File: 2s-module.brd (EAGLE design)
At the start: 100 x 80 mm, 3 parts, among them J1 CQ-USB-C16PSMT01

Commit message: build balancer prototype
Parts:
- added C1: 1nF, Capacitor:CAPC1608X85
- added C2: 22uF, Capacitor:CAPC3216X135
- added C3, C4, C5: 10nF, Capacitor:CAPC1608X85
- added JP1: PINHD-1X3, Connector:1X03
- added L1: 0630CDMCCDS-4R7MC, 0630CDMCCDS-4R7MC:0630CDMCCDS-4R7MC
- added LED1: red, adafruit:CHIPLED_0603
- added R3: 1k, resistor:R0603
- added R4: 25k, resistor:R0603
- added U1: MCP4725, SparkFun-IC-Conversion:SOT23-6
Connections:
- new net BATC: C4.2, C5.1, JP1.2, L1.P$1, LED1.C, U1.6
- new net BATP: C2.1, C4.1, JP1.1, U1.5
- new net BIAS: C3.2, U1.3
- new net ISET: C1.2, R4.2, U1.1
- new net N$1: LED1.A, R3.2
- new net SW: C3.1, L1.P$2, R3.1, U1.4
- net GND: now also C1.1, C2.2, C5.2, JP1.3, R4.1, U1.2
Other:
- board text added: "L1"

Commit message: add optocoupler
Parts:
- added TP1, TP2: TPB1,27, BeagleBone_Blue_R3:B1,27
- added U2: PC817XI, PC817XI:SOIC254P975X460-4N
- C4, C5: value 10nF -> 10uF
- turned U1 to 90 degrees
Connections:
- new net CT: TP1.TP, U2.4
- new net ET: TP2.TP, U2.3
- net BATC: now also U2.2
- net N$1: now also U2.1

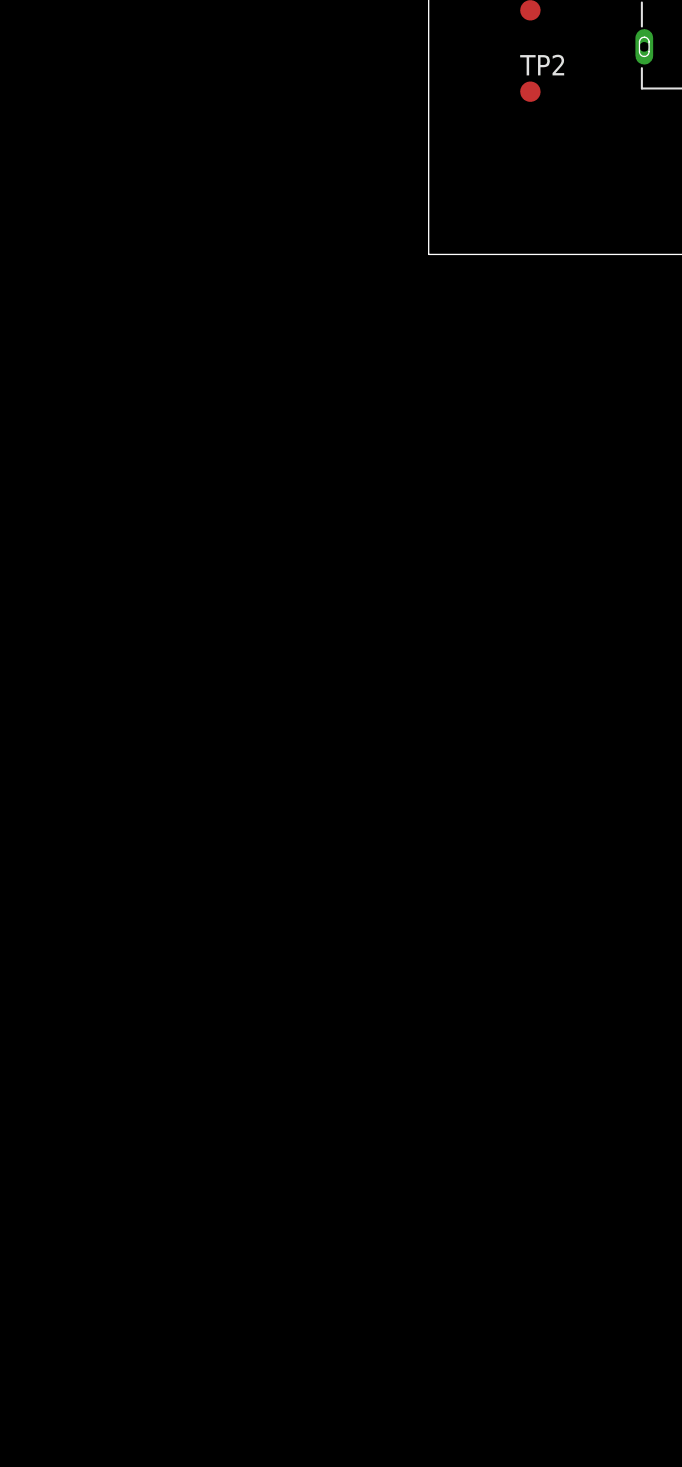
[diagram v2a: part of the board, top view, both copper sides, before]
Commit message: finish initial prototype, inductors may change
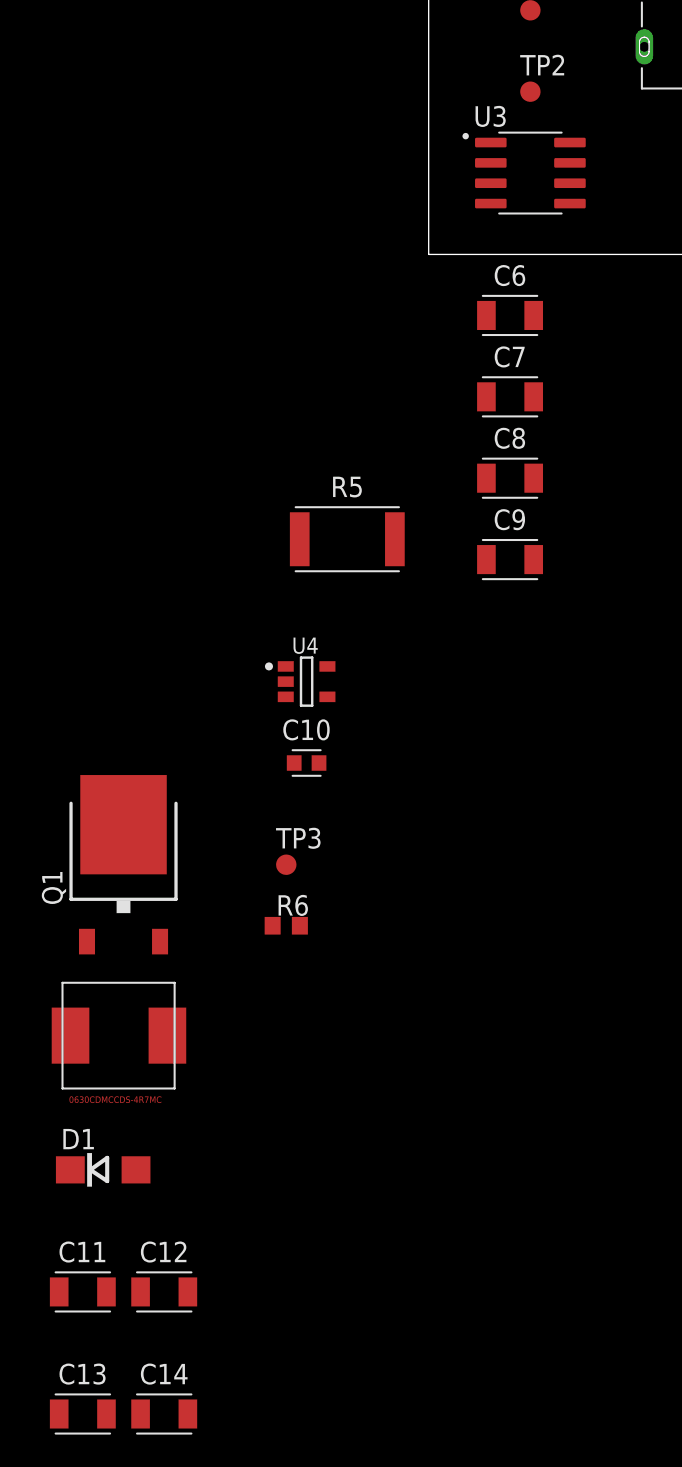
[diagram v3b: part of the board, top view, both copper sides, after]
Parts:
- added C10: 10nF, Capacitor:CAPC1608X85
- added C11, C12, C13, C14, C6, C7, C8, C9: 22uF, Capacitor:CAPC3216X135
- added D1: SS54, SS54:DO-214AC
- added L2: 0630CDMCCDS-4R7MC, 0630CDMCCDS-4R7MC:0630CDMCCDS-4R7MC
- added Q1: IRFR9020A, semiconductor:TO252
- added R5: 0.015 Ohms, Resistor:RESC6332X71
- added R6: 10k, resistor:R0603
- added TP3: TPB1,27, BeagleBone_Blue_R3:B1,27
- added U3: LM393DR, LM393DR:SOIC127P599X175-8N
- added U4: MICROCHIP_MIC5219-3_3YM5-TRMICROCHIP_MIC5219-3_3YM5-TR_0_0, Microchip - MIC5219-3.3YM5-TR:MICROCHIP_MIC5219-3_3YM5-TR_0
- C1: value 1nF -> 10nF
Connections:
- net CT renamed IS_BALANCING_C
- net ET renamed IS_BALANCING_E
- new net 3V3_ESP32_STATUS_SENSE: TP3.TP, U4.5
- new net BYP: C10.2, U4.4
- new net CSN: L2.P$1, R5.1, U3.8
- new net D: D1.A, L2.P$2, Q1.2
- new net HDRV: U3.6
- new net LDRV: Q1.1, R6.1, U3.5
- new net STAT: U3.1, U4.1, U4.3
- net BATP: now also C11.2, C12.2, C13.2, C14.2, D1.C, U3.3
- net GND: now also C10.1, C11.1, C12.1, C13.1, C14.1, C6.2, C7.2, C8.2, C9.2, Q1.3, R6.2, U3.4, U4.2
- net VBUS: now also C6.1, C7.1, C8.1, C9.1, R5.2, U3.2, U3.7

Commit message: fix some parts in sch
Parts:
- added R7: 10k, resistor:R0603
- R3: value 1k -> var
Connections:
- net 3V3_ESP32_STATUS_SENSE renamed IS_CHARGING_3V3_OUT
- net IS_BALANCING_C renamed IS_BALANCING_C_3V3_IN
- removed net IS_BALANCING_E: TP2.TP, U2.3
- new net IS_BALANCING_E_GPIO: R7.2, TP2.TP, U2.3
- net GND: now also R7.1
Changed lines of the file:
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@@
 <attribute name="VALUE" x="29.21" y="6.985" size="1.27" layer="27"/>
 </element>
-<element name="R3" library="resistor" library_urn="urn:adsk.eagle:library:348" package="R0603" package3d_urn="urn:adsk.eagle:package:23555/3" value="1k" x="25.4" y="3.81" smashed="yes">
+<element name="R3" library="resistor" library_urn="urn:adsk.eagle:library:348" package="R0603" package3d_urn="urn:adsk.eagle:package:23555/3" value="var" x="25.4" y="3.81" smashed="yes">
 <attribute name="NAME" x="24.765" y="4.445" size="1.27" layer="25"/>
 <attribute name="VALUE" x="24.765" y="1.905" size="1.27" layer="27"/>
@@
 <attribute name="VOLTAGE_RATING" value="" x="-20.32" y="-87.63" size="1.778" layer="27" display="off"/>
 </element>
+<element name="R7" library="resistor" library_urn="urn:adsk.eagle:library:348" package="R0603" package3d_urn="urn:adsk.eagle:package:23555/3" value="10k" x="-22.86" y="-78.74" smashed="yes">
+<attribute name="NAME" x="-23.495" y="-78.105" size="1.27" layer="25"/>
+<attribute name="VALUE" x="-23.495" y="-80.645" size="1.27" layer="27"/>
+</element>
 </elements>
 <signals>
@@
 <contactref element="R1" pad="2"/>
 <contactref element="R2" pad="1"/>
-<contactref element="C1" pad="1"/>
-<contactref element="R4" pad="1"/>
-<contactref element="U1" pad="2"/>
-<contactref element="JP1" pad="3"/>
-<contactref element="C2" pad="2"/>
-<contactref element="C5" pad="2"/>
 <contactref element="U3" pad="4"/>
 <contactref element="C6" pad="2"/>
@@
 <contactref element="C10" pad="1"/>
 <contactref element="R6" pad="2"/>
+<contactref element="C1" pad="1"/>
+<contactref element="R4" pad="1"/>
+<contactref element="U1" pad="2"/>
+<contactref element="JP1" pad="3"/>
+<contactref element="C2" pad="2"/>
+<contactref element="C5" pad="2"/>
+<contactref element="R7" pad="1"/>
+<wire x1="-23.0654" y1="-72.39" x2="-23.71" y2="-78.74" width="0" layer="19" extent="1-1"/>
 <wire x1="-17.9854" y1="-72.39" x2="-23.0654" y2="-72.39" width="0" layer="19" extent="1-1"/>
 <wire x1="-23.0654" y1="-64.77" x2="-23.0654" y2="-72.39" width="0" layer="19" extent="1-1"/>
@@
 <wire x1="8.41" y1="25.4" x2="26.25" y2="3.81" width="0" layer="19" extent="1-1"/>
 </signal>
-<signal name="IS_BALANCING_C">
+<signal name="IS_BALANCING_C_3V3_IN">
 <contactref element="U2" pad="4"/>
 <contactref element="TP1" pad="TP"/>
 <wire x1="6.35" y1="15.24" x2="16.99" y2="25.4" width="0" layer="19" extent="1-1"/>
 </signal>
-<signal name="IS_BALANCING_E">
+<signal name="IS_BALANCING_E_GPIO">
 <contactref element="U2" pad="3"/>
 <contactref element="TP2" pad="TP"/>
-<wire x1="6.35" y1="10.16" x2="16.99" y2="22.86" width="0" layer="19" extent="1-1"/>
+<contactref element="R7" pad="2"/>
+<wire x1="6.35" y1="10.16" x2="-22.01" y2="-78.74" width="0" layer="19" extent="1-1"/>
+<wire x1="16.99" y1="22.86" x2="6.35" y2="10.16" width="0" layer="19" extent="1-1"/>
 </signal>
 <signal name="CSN">
@@
 <wire x1="-6.32" y1="-27.62" x2="-6.8454" y2="-31.75" width="0" layer="19" extent="1-1"/>
 </signal>
-<signal name="3V3_ESP32_STATUS_SENSE">
+<signal name="IS_CHARGING_3V3_OUT">
 <contactref element="U4" pad="5"/>
 <contactref element="TP3" pad="TP"/>

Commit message: build board to be wired
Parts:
- added L3: 2.2uH, 74437368047:INDM110100X380N
- L1: value 0630CDMCCDS-4R7MC -> (none)
- L2: value 0630CDMCCDS-4R7MC -> 2.2uH
- moved C13 135.4 mm to (11.8, 58.8)
- moved C14 131.9 mm to (11.8, 56.4)
- moved C12 131.5 mm to (11.8, 63.6)
- moved C11 130.3 mm to (11.8, 61.2)
- moved D1 127.2 mm to (19.3, 63.8)
- moved TP3 111.1 mm to (33.0, 64.8)
- moved Q1 109.3 mm to (25.7, 61.6)
- moved R7 100.6 mm to (8.51, 16.9)
- moved C10 96.5 mm to (44.2, 49.7)
- moved R6 95.5 mm to (23.6, 47.9)
- moved R5 91.3 mm to (43.2, 59.7)
- moved L2 87.2 mm to (7.24, 29.7)
- moved C9 81.4 mm to (38.1, 55.4)
- moved U4 80.8 mm to (15.9, 50.7)
- moved TP2 80.2 mm to (72.8, 55.1)
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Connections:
- net CSN: now also L3.2
- net D: now also L3.1
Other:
- board text added: "C2"
- board text added: "L2"

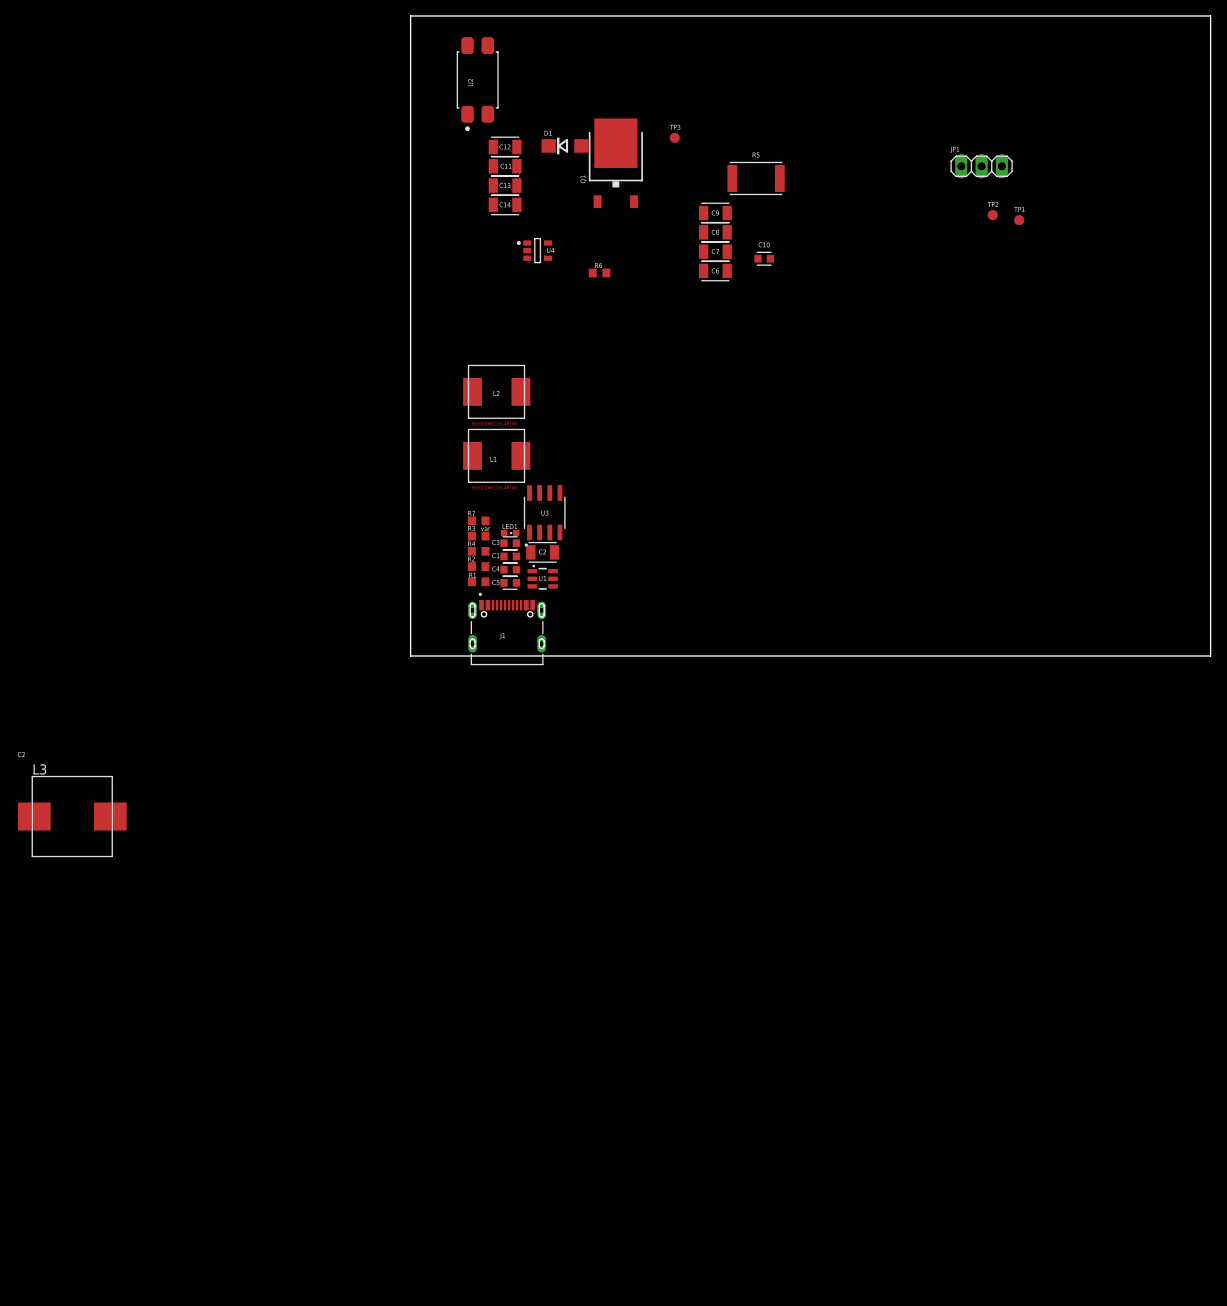
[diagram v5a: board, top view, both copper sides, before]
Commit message: add alternative direction indicators
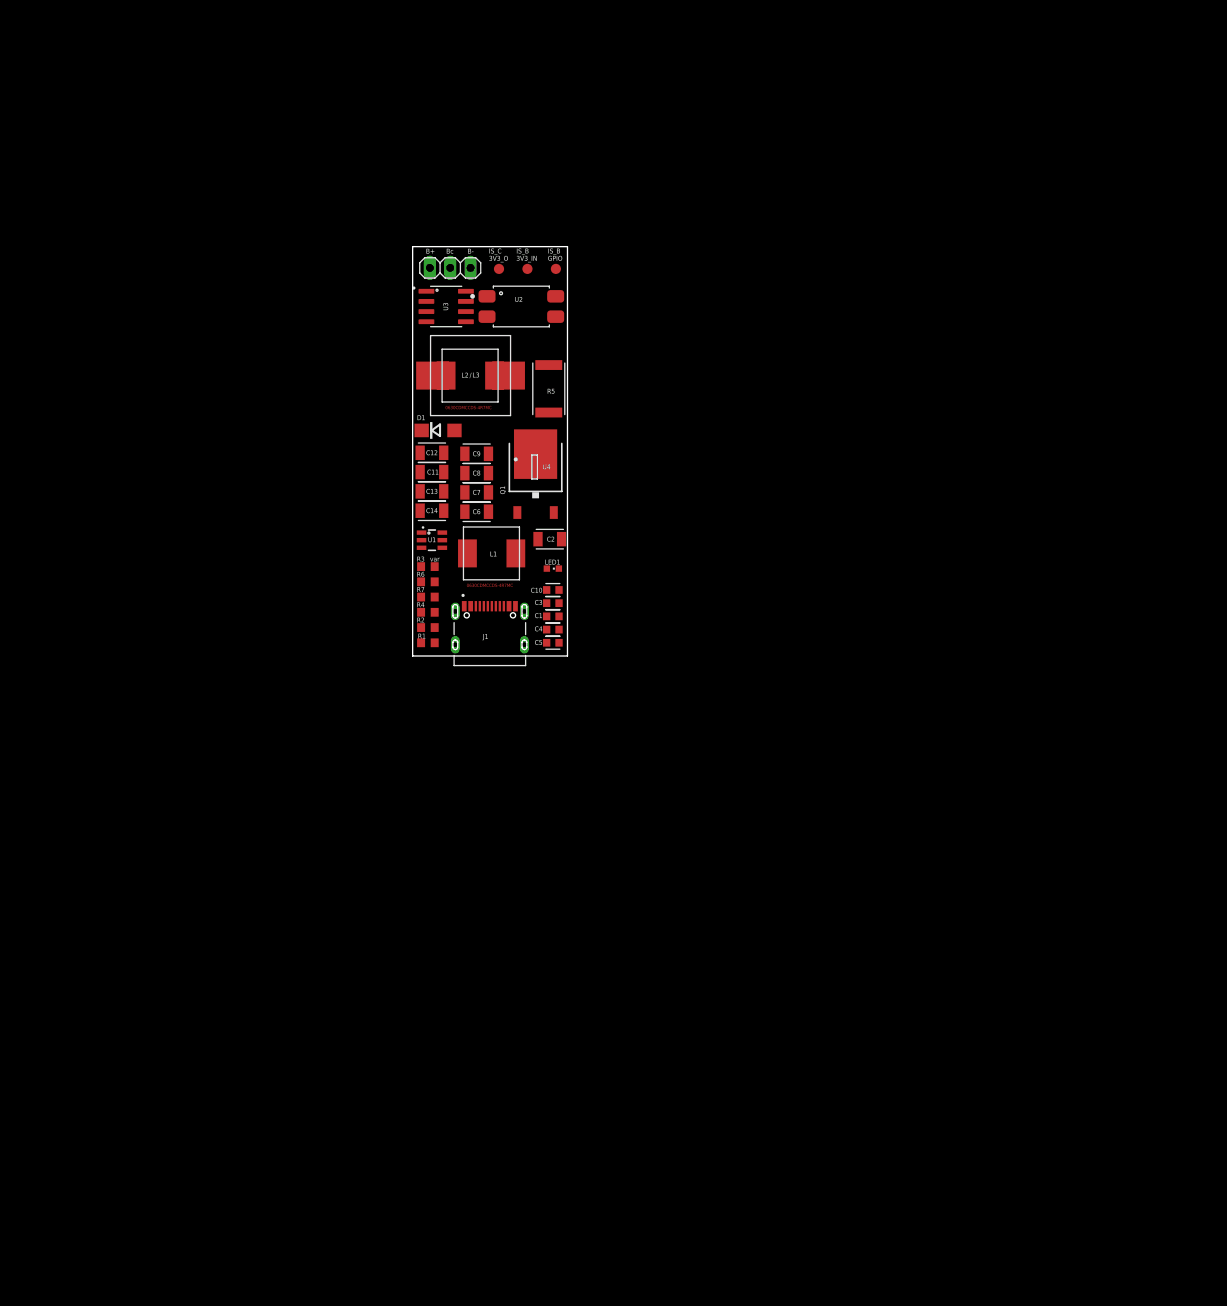
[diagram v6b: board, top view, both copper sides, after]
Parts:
- moved L3 74.3 mm to (7.49, 35.1)
- moved JP1 67.6 mm to (4.95, 48.5)
- moved TP1 61.8 mm to (14.6, 48.4)
- moved TP2 55.0 mm to (18.2, 48.4)
- moved C10 49.1 mm to (17.8, 8.26)
- moved R6 44.2 mm to (2.16, 9.27)
- moved C6 42.4 mm to (8.26, 18.0)
- moved C8 42.4 mm to (8.26, 22.9)
- moved C7 42.4 mm to (8.26, 20.4)
- moved C9 42.4 mm to (8.26, 25.3)
- moved Q1 40.1 mm to (15.6, 22.7)
- moved C11 39.3 mm to (2.67, 23.0)
- moved C12 39.3 mm to (2.67, 25.4)
- moved C13 39.3 mm to (2.67, 20.6)
- moved C14 39.3 mm to (2.67, 18.2)
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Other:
- board size 100 x 80 mm -> 19.4 x 51.2 mm
- board text added: "/"
- board text added: "B+"
- board text added: "B-"
- board text added: "Bc"
- board text added: "IS_B 3V3_IN"
- board text added: "IS_B GPIO"
- board text added: "IS_C 3V3_O"
- board text removed: "C2"

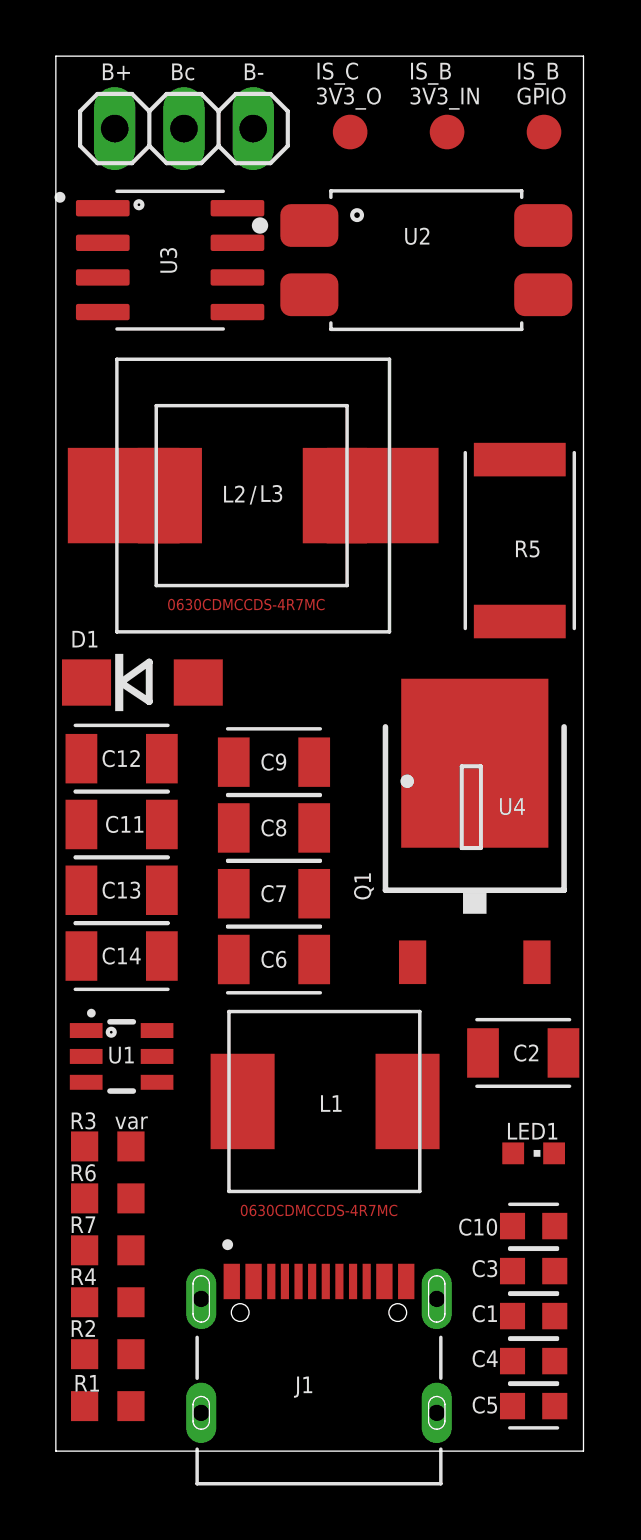
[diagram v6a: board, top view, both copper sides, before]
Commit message: rearrange more to save space
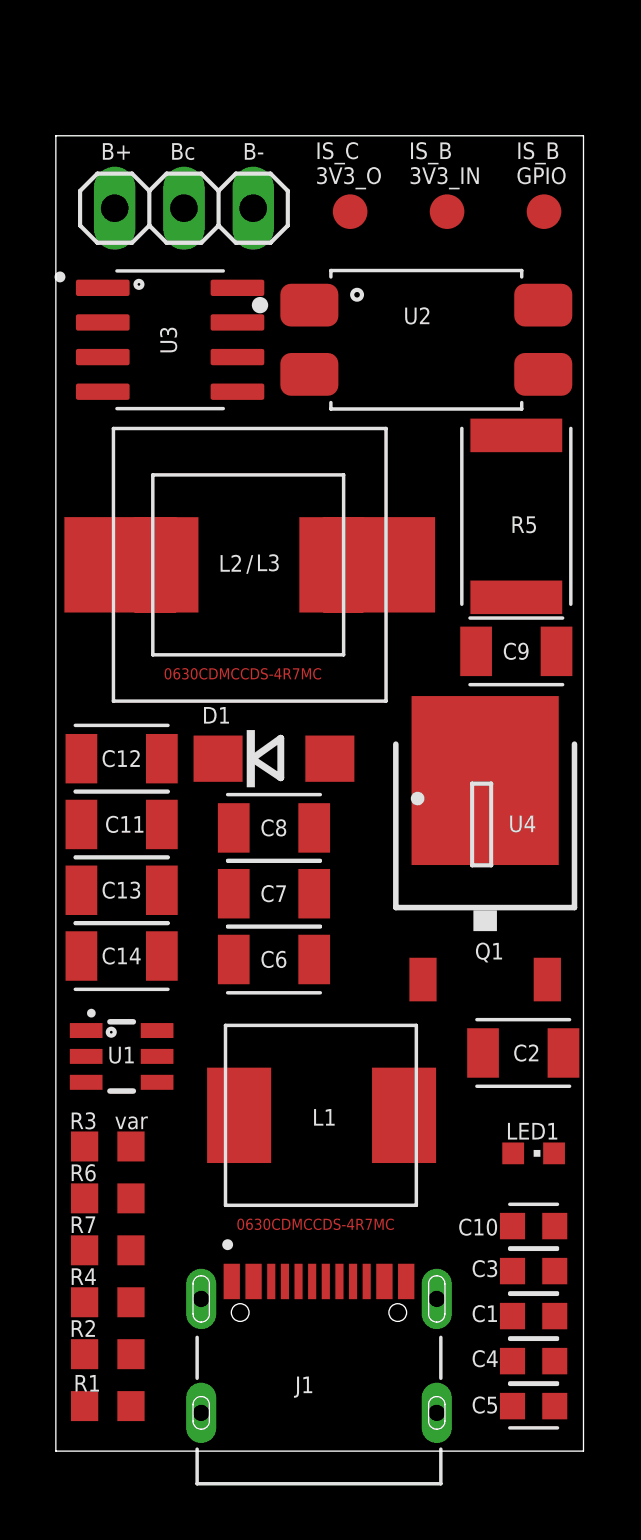
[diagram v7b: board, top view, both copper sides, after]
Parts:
- moved C9 9.77 mm to (17.1, 29.3)
- moved D1 5.58 mm to (8.26, 25.4)
- moved JP1 2.92 mm to (4.95, 45.6)
- moved TP1 2.92 mm to (14.6, 45.5)
- moved TP2 2.92 mm to (18.2, 45.5)
- moved TP3 2.92 mm to (11.0, 45.5)
- moved U2 2.92 mm to (13.8, 40.8)
- moved U3 2.92 mm to (4.45, 40.8)
- moved L2 2.54 mm to (3.81, 29.2)
- moved L3 2.54 mm to (7.37, 32.5)
- moved R5 0.90 mm to (17.1, 34.3)
- moved U4 0.74 mm to (15.9, 23.0)
- moved Q1 0.74 mm to (16.0, 22.1)
- moved L1 0.52 mm to (6.48, 9.02)
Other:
- board size 19.4 x 51.2 mm -> 19.4 x 48.2 mm
